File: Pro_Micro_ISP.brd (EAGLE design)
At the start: 17.8 x 53.3 mm, 9 parts

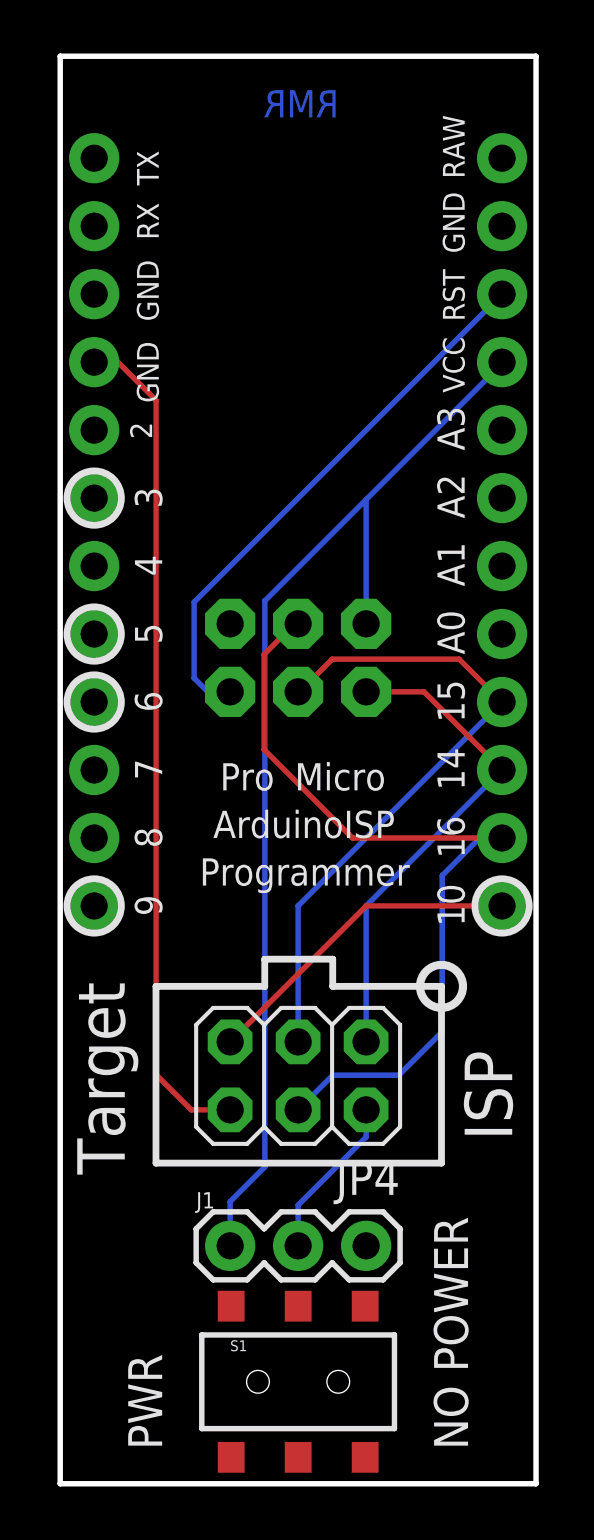
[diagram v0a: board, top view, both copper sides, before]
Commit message: Add files via upload
Fixed missing traces to SMD switch. Minor changes to silkscreen.
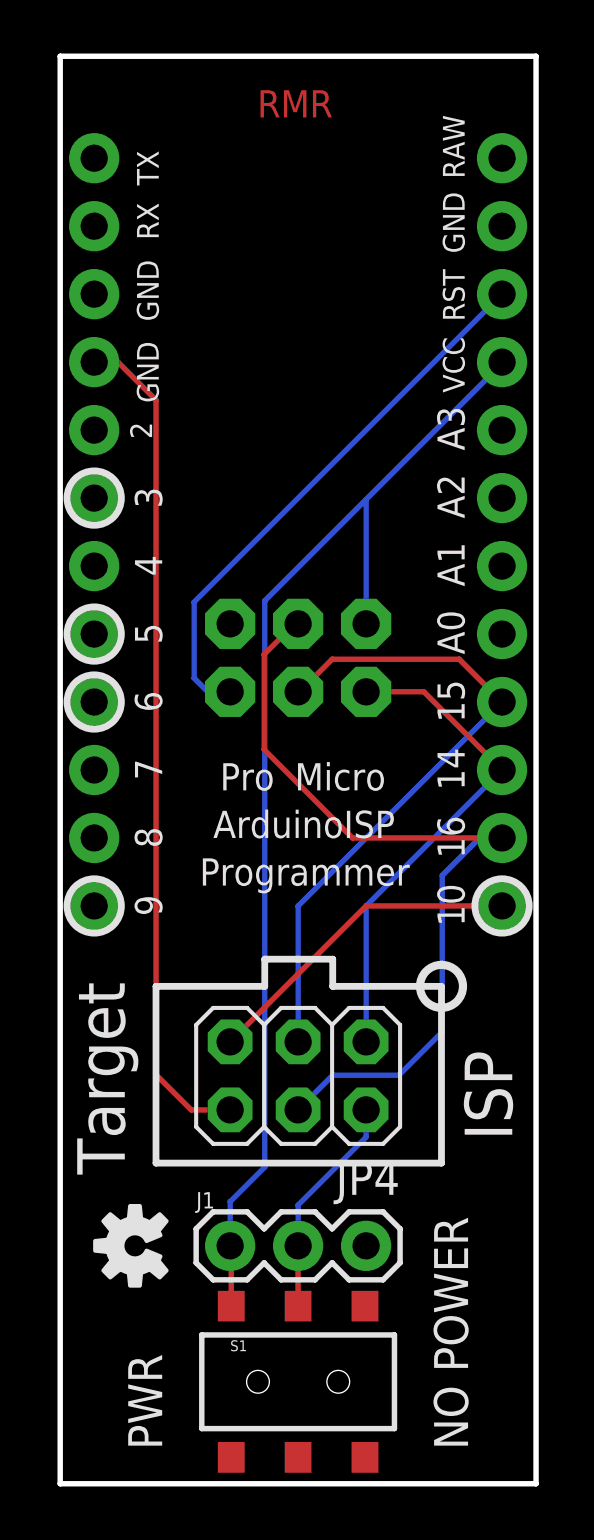
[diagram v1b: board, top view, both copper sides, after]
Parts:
- flipped U$3 to the top
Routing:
- net VCC: track 41.9 -> 44.1 mm
- net N$14: track 6.13 -> 8.39 mm
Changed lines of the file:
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@@
 <circle x="1.27" y="1.27" radius="1.016" width="0.254" layer="21"/>
 <circle x="16.51" y="1.27" radius="1.016" width="0.254" layer="21"/>
-<text x="10.414" y="30.734" size="1.016" layer="16" ratio="25" rot="MR0">RMR</text>
+<text x="7.366" y="30.734" size="1.016" layer="1" ratio="25">RMR</text>
 <text x="3.81" y="0.889" size="1.016" layer="21" ratio="15" rot="R90">9</text>
 <text x="3.81" y="3.429" size="1.016" layer="21" ratio="15" rot="R90">8</text>
@@
 <text x="5.715" y="3.81" size="1.016" layer="21" ratio="15">ArduinoISP</text>
 <text x="15.113" y="23.114" size="0.8128" layer="21" ratio="15" rot="R90">RST</text>
-<text x="12.065" y="5.461" size="1.016" layer="22" ratio="15" rot="MR0">32U4 ISP</text>
+<text x="14.097" y="5.461" size="1.778" layer="22" ratio="15" rot="MR0">32U4 ISP</text>
 <text x="2.413" y="-8.763" size="1.778" layer="21" rot="R90">Target</text>
 </plain>
@@
 <attribute name="VALUE" x="-1.905" y="0" size="1.27" layer="28" rot="MR90"/>
 </element>
-<element name="U$3" library="SparkFun" package="OSHW-LOGO-S" value="OSHW-LOGOS" x="2.794" y="-11.43" smashed="yes" rot="MR90"/>
+<element name="U$3" library="SparkFun" package="OSHW-LOGO-S" value="OSHW-LOGOS" x="2.794" y="-11.43" smashed="yes" rot="R90"/>
 <element name="FRAME1" library="SparkFun-Aesthetics" package="CREATIVE_COMMONS" value="FRAME-LETTER" x="-9.632121875" y="38.1" smashed="yes"/>
 <element name="S1" library="SparkFun" package="AYZ0202" value="Power Select" x="8.89" y="-16.51" smashed="yes">
@@
 <wire x1="11.43" y1="16.4562125" x2="16.51" y2="21.5362125" width="0.2032" layer="16"/>
 <wire x1="11.43" y1="11.811" x2="11.43" y2="16.4562125" width="0.2032" layer="16"/>
-<wire x1="6.35" y1="-11.43" x2="6.39" y2="-13.685" width="0" layer="19" extent="1-1"/>
+<wire x1="6.39" y1="-13.685" x2="6.39" y2="-11.47" width="0.2032" layer="1"/>
+<wire x1="6.39" y1="-11.47" x2="6.35" y2="-11.43" width="0.2032" layer="1"/>
 </signal>
 <signal name="RAW" class="1">
@@
 <wire x1="11.43" y1="-7.366" x2="8.89" y2="-9.906" width="0.2032" layer="16"/>
 <wire x1="8.89" y1="-9.906" x2="8.89" y2="-11.43" width="0.2032" layer="16"/>
-<wire x1="8.89" y1="-11.43" x2="8.89" y2="-13.685" width="0" layer="19" extent="1-1"/>
+<wire x1="8.89" y1="-13.685" x2="8.89" y2="-11.43" width="0.2032" layer="1"/>
 </signal>
 </signals>
